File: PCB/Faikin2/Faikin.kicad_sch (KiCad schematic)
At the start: 33 parts, among them J1 1x5, J2 Shelly, Q1 BSS138PS, U2 Barcode, U2 ESP32-S3-MINI-1, U3 MD8942

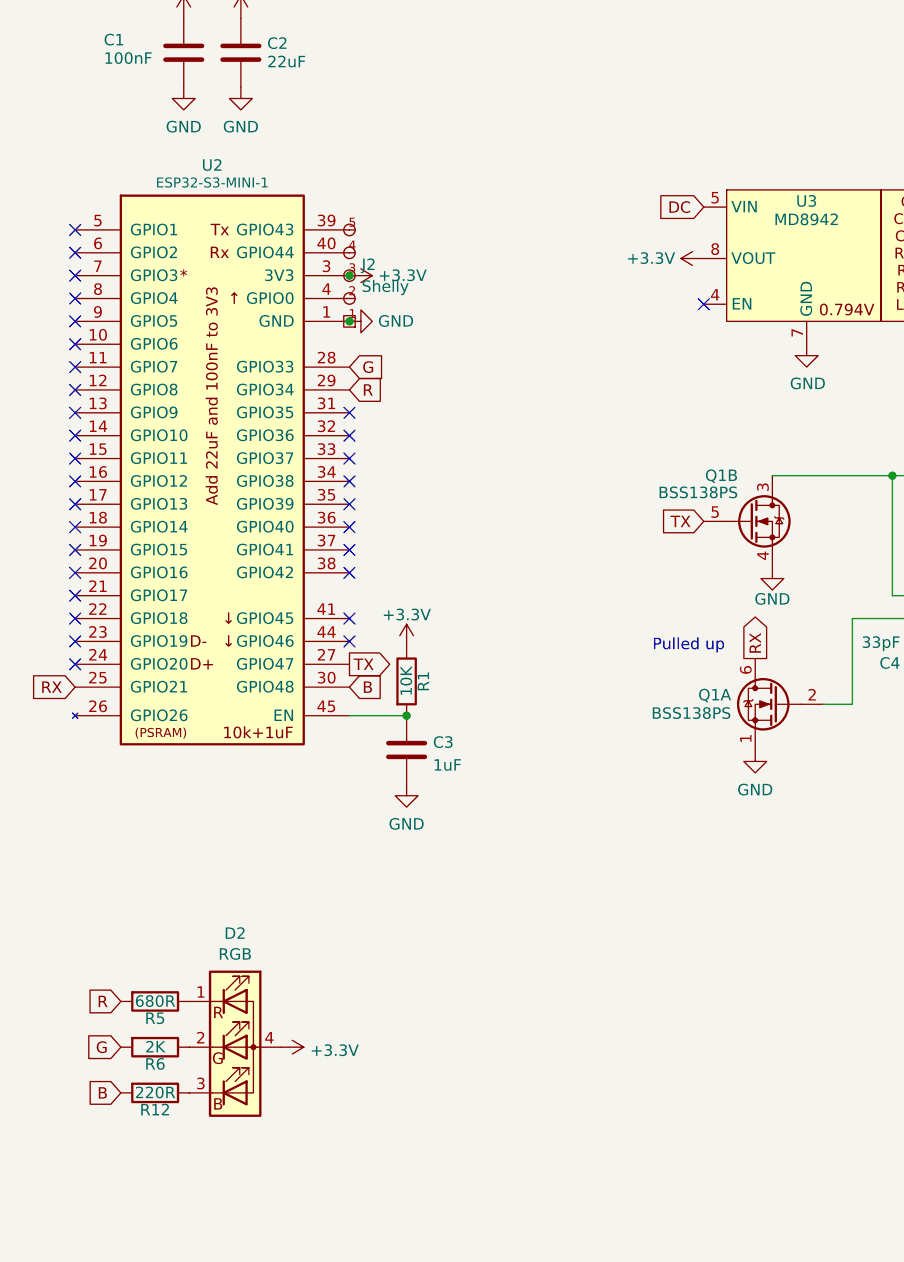
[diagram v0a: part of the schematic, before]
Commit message: Revised for USB connector as well
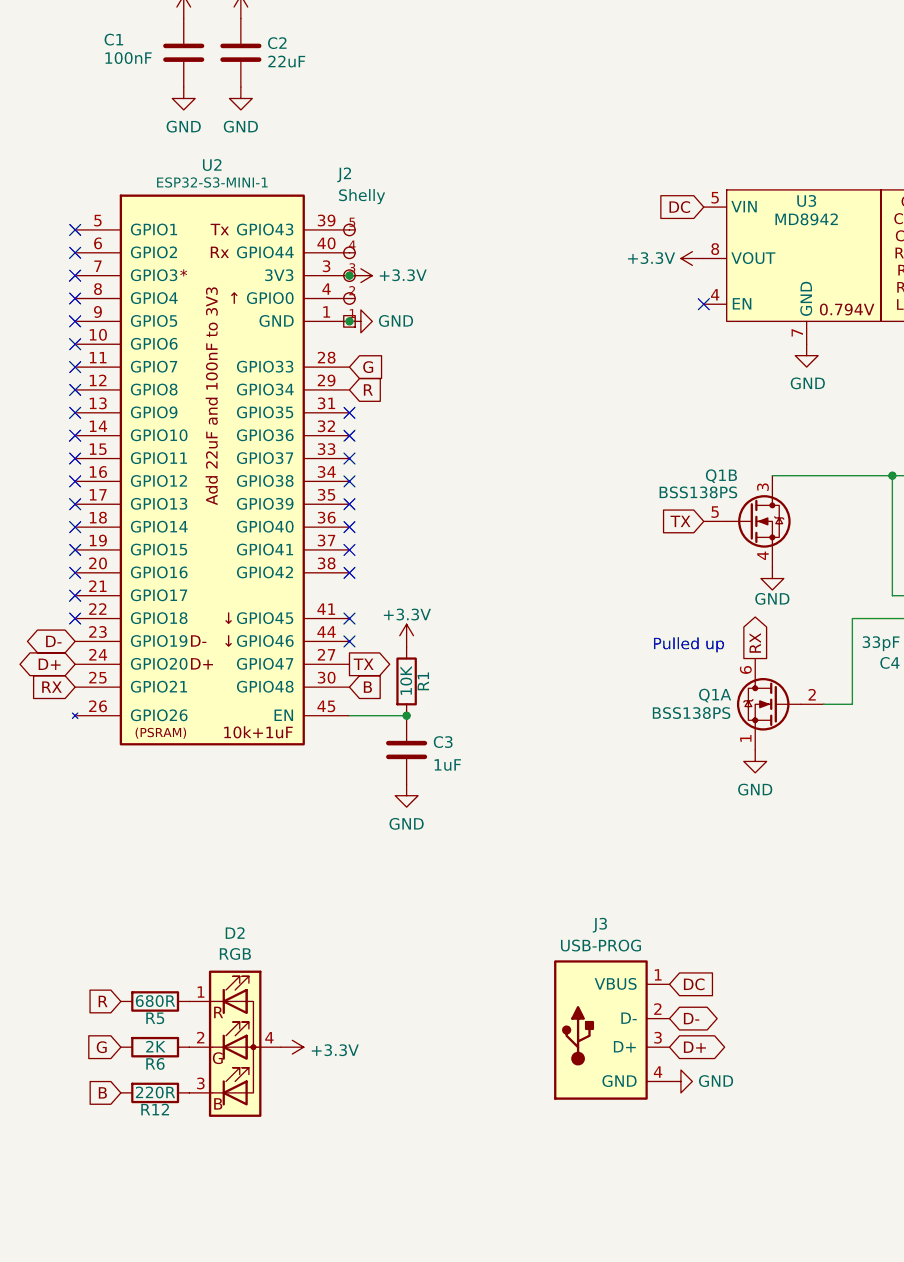
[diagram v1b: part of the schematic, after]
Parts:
- added J3: USB-PROG, RevK:USB-PROG, symbol RevK:USB-PROG
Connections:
- net DC: now also J3.1 (VBUS)
- net GND: now also J3.4 (GND)
- net D-: now reaches U2.23 (GPIO19)
- net D-: now also J3.2 (D-)
- net D+: now reaches U2.24 (GPIO20)
- net D+: now also J3.3 (D+)
- no-connect marks 31 -> 29
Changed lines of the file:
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@@
   (no_connect (at 79.375 71.12))
   (no_connect (at 48.895 60.96))
-  (no_connect (at 48.895 96.52))
   (no_connect (at 79.375 91.44))
   (no_connect (at 48.895 58.42))
@@
   (no_connect (at 48.895 78.74))
   (no_connect (at 48.895 76.2))
-  (no_connect (at 48.895 93.98))
   (no_connect (at 48.895 71.12))
   (no_connect (at 48.895 48.26))
@@
     (effects (font (size 1.27 1.27)) (justify left bottom))
   )
+  (global_label "DC" (shape input) (at 114.935 132.08 0) (fields_autoplaced)
+    (effects (font (size 1.27 1.27)) (justify left))
+    (property "Intersheetrefs" "${INTERSHEET_REFS}" (at 119.806 132.08 0)
+      (effects (font (size 1.27 1.27)) (justify left) hide)
+    )
+  )
+  (global_label "D-" (shape bidirectional) (at 48.895 93.98 180) (fields_autoplaced)
+    (effects (font (size 1.27 1.27)) (justify right))
+    (property "Intersheetrefs" "${INTERSHEET_REFS}" (at 42.7691 93.98 0)
+      (effects (font (size 1.27 1.27)) (justify right) hide)
+    )
+  )
   (global_label "G" (shape input) (at 79.375 63.5 0) (fields_autoplaced)
     (effects (font (size 1.27 1.27)) (justify left))
@@
     )
   )
+  (global_label "D+" (shape bidirectional) (at 48.895 96.52 180) (fields_autoplaced)
+    (effects (font (size 1.27 1.27)) (justify right))
+    (property "Intersheetrefs" "${INTERSHEET_REFS}" (at 42.7691 96.52 0)
+      (effects (font (size 1.27 1.27)) (justify right) hide)
+    )
+  )
   (global_label "TX" (shape input) (at 118.745 80.645 180) (fields_autoplaced)
     (effects (font (size 1.27 1.27)) (justify right))
@@
     )
   )
+  (global_label "D+" (shape bidirectional) (at 114.935 139.065 0) (fields_autoplaced)
+    (effects (font (size 1.27 1.27)) (justify left))
+    (property "Intersheetrefs" "${INTERSHEET_REFS}" (at 121.0609 139.065 0)
+      (effects (font (size 1.27 1.27)) (justify left) hide)
+    )
+  )
   (global_label "DC" (shape output) (at 161.29 86.36 180) (fields_autoplaced)
     (effects (font (size 1.27 1.27)) (justify right))
@@
     )
   )
+  (global_label "D-" (shape bidirectional) (at 114.935 135.89 0) (fields_autoplaced)
+    (effects (font (size 1.27 1.27)) (justify left))
+    (property "Intersheetrefs" "${INTERSHEET_REFS}" (at 121.0609 135.89 0)
+      (effects (font (size 1.27 1.27)) (justify left) hide)
+    )
+  )
   (global_label "RX" (shape input) (at 48.895 99.06 180) (fields_autoplaced)
     (effects (font (size 1.27 1.27)) (justify right))
@@
   )
   (symbol (lib_id "RevK:Shelly") (at 79.375 53.34 0) (unit 1)
-    (in_bom no) (on_board yes) (dnp no) (fields_autoplaced)
-    (property "Reference" "J2" (at 80.7212 52.1279 0)
-      (effects (font (size 1.27 1.27)) (justify left))
-    )
-    (property "Value" "Shelly" (at 80.7212 54.5521 0)
+    (in_bom no) (on_board yes) (dnp no)
+    (property "Reference" "J2" (at 78.105 42.0258 0)
+      (effects (font (size 1.27 1.27)) (justify left))
+    )
+    (property "Value" "Shelly" (at 78.105 44.45 0)
       (effects (font (size 1.27 1.27)) (justify left))
     )
@@
         (path "/46c350bb-7de4-4e81-aafd-4af55e37aab0"
           (reference "V4") (unit 1)
+        )
+      )
+    )
+  )
+  (symbol (lib_id "RevK:USB-PROG") (at 107.315 137.16 0) (unit 1)
+    (in_bom yes) (on_board yes) (dnp no) (fields_autoplaced)
+    (property "Reference" "J3" (at 107.315 125.3957 0)
+      (effects (font (size 1.27 1.27)))
+    )
+    (property "Value" "USB-PROG" (at 107.315 127.8199 0)
+      (effects (font (size 1.27 1.27)))
+    )
+    (property "Footprint" "RevK:USB-PROG" (at 111.125 138.43 0)
+      (effects (font (size 1.27 1.27)) hide)
+    )
+    (property "Datasheet" " ~" (at 111.125 138.43 0)
+      (effects (font (size 1.27 1.27)) hide)
+    )
+    (pin "1")
+    (pin "2")
+    (pin "3")
+    (pin "4")
+    (instances
+      (project "Faikin"
+        (path "/46c350bb-7de4-4e81-aafd-4af55e37aab0"
+          (reference "J3") (unit 1)
         )
       )
@@
         )
       )
+    )
+  )
+  (symbol (lib_id "power:GND") (at 114.935 142.875 90) (unit 1)
+    (in_bom yes) (on_board yes) (dnp no) (fields_autoplaced)
+    (property "Reference" "#PWR0105" (at 121.285 142.875 0)
+      (effects (font (size 1.27 1.27)) hide)
+    )
+    (property "Value" "GND" (at 118.11 142.875 90)
+      (effects (font (size 1.27 1.27)) (justify right))
+    )
+    (property "Footprint" "" (at 114.935 142.875 0)
+      (effects (font (size 1.27 1.27)) hide)
+    )
+    (property "Datasheet" "" (at 114.935 142.875 0)
+      (effects (font (size 1.27 1.27)) hide)
+    )
+    (pin "1")
+    (instances
+      (project "USBA"
+        (path "/2d210a96-f81f-42a9-8bf4-1b43c11086f3"
+          (reference "#PWR0105") (unit 1)
+        )
+      )
+      (project "Faikin"
+        (path "/46c350bb-7de4-4e81-aafd-4af55e37aab0"
+          (reference "#PWR016") (unit 1)
+        )
+      )

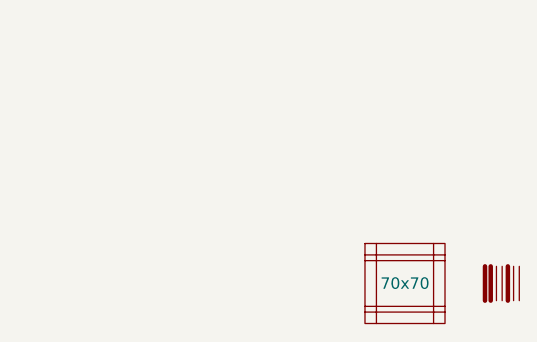
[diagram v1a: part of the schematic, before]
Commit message: Could not do larger board outline
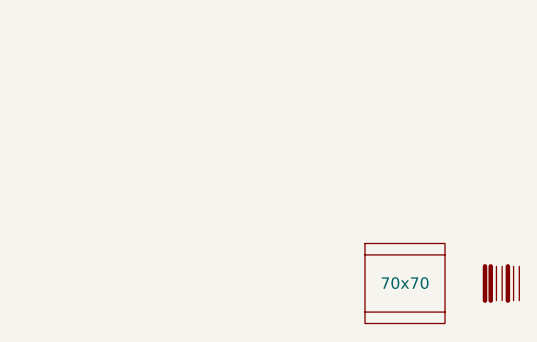
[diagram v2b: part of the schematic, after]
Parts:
- removed V3, V4, V5, V6: ~, RevK:VCUT70, symbol RevK:VCUT
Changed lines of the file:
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@@
-    )
-  )
-  (symbol (lib_id "RevK:VCUT") (at 259.08 174.625 270) (unit 1)
-    (in_bom no) (on_board yes) (dnp no) (fields_autoplaced)
-    (property "Reference" "V4" (at 260.35 174.625 0)
-      (effects (font (size 1.27 1.27)) hide)
-    )
-    (property "Value" "~" (at 259.08 174.625 0)
-      (effects (font (size 1.27 1.27)))
-    )
-    (property "Footprint" "RevK:VCUT70" (at 257.81 174.625 0)
-      (effects (font (size 1.27 1.27)) hide)
-    )
-    (property "Datasheet" "" (at 259.08 174.625 0)
-      (effects (font (size 1.27 1.27)) hide)
-    )
-    (property "Sim.Enable" "0" (at 259.08 174.625 0)
-      (effects (font (size 1.27 1.27)) hide)
-    )
-    (instances
-      (project "Faikin"
-        (path "/46c350bb-7de4-4e81-aafd-4af55e37aab0"
-          (reference "V4") (unit 1)
-        )
-      )
     )
   )
@@
         (path "/46c350bb-7de4-4e81-aafd-4af55e37aab0"
           (reference "J3") (unit 1)
-        )
-      )
-    )
-  )
-  (symbol (lib_id "RevK:VCUT") (at 262.255 177.165 180) (unit 1)
-    (in_bom no) (on_board yes) (dnp no) (fields_autoplaced)
-    (property "Reference" "V6" (at 262.255 178.435 0)
-      (effects (font (size 1.27 1.27)) hide)
-    )
-    (property "Value" "~" (at 262.255 177.165 0)
-      (effects (font (size 1.27 1.27)))
-    )
-    (property "Footprint" "RevK:VCUT70" (at 262.255 175.895 0)
-      (effects (font (size 1.27 1.27)) hide)
-    )
-    (property "Datasheet" "" (at 262.255 177.165 0)
-      (effects (font (size 1.27 1.27)) hide)
-    )
-    (property "Sim.Enable" "0" (at 262.255 177.165 0)
-      (effects (font (size 1.27 1.27)) hide)
-    )
-    (instances
-      (project "Faikin"
-        (path "/46c350bb-7de4-4e81-aafd-4af55e37aab0"
-          (reference "V6") (unit 1)
         )
       )
@@
         (path "/46c350bb-7de4-4e81-aafd-4af55e37aab0"
           (reference "C6") (unit 1)
-        )
-      )
-    )
-  )
-  (symbol (lib_id "RevK:VCUT") (at 262.255 172.085 0) (unit 1)
-    (in_bom no) (on_board yes) (dnp no) (fields_autoplaced)
-    (property "Reference" "V5" (at 262.255 170.815 0)
-      (effects (font (size 1.27 1.27)) hide)
-    )
-    (property "Value" "~" (at 262.255 172.085 0)
-      (effects (font (size 1.27 1.27)))
-    )
-    (property "Footprint" "RevK:VCUT70" (at 262.255 173.355 0)
-      (effects (font (size 1.27 1.27)) hide)
-    )
-    (property "Datasheet" "" (at 262.255 172.085 0)
-      (effects (font (size 1.27 1.27)) hide)
-    )
-    (property "Sim.Enable" "0" (at 262.255 172.085 0)
-      (effects (font (size 1.27 1.27)) hide)
-    )
-    (instances
-      (project "Faikin"
-        (path "/46c350bb-7de4-4e81-aafd-4af55e37aab0"
-          (reference "V5") (unit 1)
         )
       )
@@
         )
       )
-    )
-  )
-  (symbol (lib_id "RevK:VCUT") (at 265.43 174.625 270) (unit 1)
-    (in_bom no) (on_board yes) (dnp no) (fields_autoplaced)
-    (property "Reference" "V3" (at 266.7 174.625 0)
-      (effects (font (size 1.27 1.27)) hide)
-    )
-    (property "Value" "~" (at 265.43 174.625 0)
-      (effects (font (size 1.27 1.27)))
-    )
-    (property "Footprint" "RevK:VCUT70" (at 264.16 174.625 0)
-      (effects (font (size 1.27 1.27)) hide)
-    )
-    (property "Datasheet" "" (at 265.43 174.625 0)
-      (effects (font (size 1.27 1.27)) hide)
-    )
-    (property "Sim.Enable" "0" (at 265.43 174.625 0)
-      (effects (font (size 1.27 1.27)) hide)
-    )
-    (instances
-      (project "Faikin"
-        (path "/46c350bb-7de4-4e81-aafd-4af55e37aab0"
-          (reference "V3") (unit 1)
-        )
-      )

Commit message: Extra cut outs
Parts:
- removed U2: Barcode, RevK:EAN-5060634238151, symbol RevK:Barcode
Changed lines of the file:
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@@
-    )
-  )
-  (symbol (lib_id "RevK:Barcode") (at 273.05 174.625 0) (unit 1)
-    (in_bom no) (on_board yes) (dnp no) (fields_autoplaced)
-    (property "Reference" "U2" (at 273.05 177.8 0)
-      (effects (font (size 1.27 1.27)) hide)
-    )
-    (property "Value" "Barcode" (at 273.05 179.705 0)
-      (effects (font (size 1.27 1.27)) hide)
-    )
-    (property "Footprint" "RevK:EAN-5060634238151" (at 272.415 175.26 0)
-      (effects (font (size 1.27 1.27)) hide)
-    )
-    (property "Datasheet" "" (at 272.415 175.26 0)
-      (effects (font (size 1.27 1.27)) hide)
-    )
-    (property "Note" "Non part, PCB printed" (at 273.05 168.91 0)
-      (effects (font (size 1.27 1.27)) hide)
-    )
-    (instances
-      (project "Faikin"
-        (path "/46c350bb-7de4-4e81-aafd-4af55e37aab0"
-          (reference "U2") (unit 1)
-        )
-      )
     )
   )

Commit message: Pull up
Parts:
- added R1: 10K, RevK:R_0402, symbol Device:R
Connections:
- net +3.3V: now also R1.1
- net RX: now also R1.2
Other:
- note removed: "Pulled up"
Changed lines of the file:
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@@
   (junction (at 79.375 58.42) (diameter 0) (color 0 0 0 0)
+  )
+  (junction (at 117.475 95.885) (diameter 0) (color 0 0 0 0)
   )
   (junction (at 139.7 75.565) (diameter 0) (color 0 0 0 0)
@@
     (stroke (width 0) (type default))
   )
+  (wire (pts (xy 117.475 95.885) (xy 124.46 95.885))
+    (stroke (width 0) (type default))
+  )
+  (wire (pts (xy 113.03 95.885) (xy 117.475 95.885))
+    (stroke (width 0) (type default))
+  )
   (wire (pts (xy 157.48 88.9) (xy 161.29 88.9))
     (stroke (width 0) (type default))
@@
   (wire (pts (xy 143.51 91.44) (xy 149.86 91.44))
     (stroke (width 0) (type default))
-  )
-  (text "Pulled up" (at 113.03 95.25 0)
-    (effects (font (size 1.27 1.27)) (justify left bottom))
   )
   (global_label "DC" (shape input) (at 114.935 132.08 0) (fields_autoplaced)
@@
     )
   )
-  (global_label "RX" (shape output) (at 124.46 95.885 90) (fields_autoplaced)
-    (effects (font (size 1.27 1.27)) (justify left))
-    (property "Intersheetrefs" "${INTERSHEET_REFS}" (at 124.3806 91.0813 90)
-      (effects (font (size 1.27 1.27)) (justify left) hide)
+  (global_label "RX" (shape output) (at 113.03 95.885 180) (fields_autoplaced)
+    (effects (font (size 1.27 1.27)) (justify right))
+    (property "Intersheetrefs" "${INTERSHEET_REFS}" (at 108.2195 95.885 0)
+      (effects (font (size 1.27 1.27)) (justify right) hide)
     )
   )
@@
         (path "/46c350bb-7de4-4e81-aafd-4af55e37aab0"
           (reference "#PWR05") (unit 1)
+        )
+      )
+    )
+  )
+  (symbol (lib_id "Device:R") (at 117.475 92.075 0) (unit 1)
+    (in_bom yes) (on_board yes) (dnp no)
+    (property "Reference" "R1" (at 119.38 92.075 90)
+      (effects (font (size 1.27 1.27)))
+    )
+    (property "Value" "10K" (at 117.475 92.075 90)
+      (effects (font (size 1.27 1.27)))
+    )
+    (property "Footprint" "RevK:R_0402" (at 115.697 92.075 90)
+      (effects (font (size 1.27 1.27)) hide)
+    )
+    (property "Datasheet" "~" (at 117.475 92.075 0)
+      (effects (font (size 1.27 1.27)) hide)
+    )
+    (pin "1")
+    (pin "2")
+    (instances
+      (project "USBA"
+        (path "/2d210a96-f81f-42a9-8bf4-1b43c11086f3"
+          (reference "R1") (unit 1)
+        )
+      )
+      (project "Faikin"
+        (path "/46c350bb-7de4-4e81-aafd-4af55e37aab0"
+          (reference "R4") (unit 1)
+        )
+      )
+      (project "Reference"
+        (path "/825c70b0-4860-42b7-97dc-86bfa46e06fd"
+          (reference "R7") (unit 1)
         )
       )
@@
         )
       )
+    )
+  )
+  (symbol (lib_id "power:+3.3V") (at 117.475 88.265 0) (unit 1)
+    (in_bom yes) (on_board yes) (dnp no) (fields_autoplaced)
+    (property "Reference" "#PWR0106" (at 117.475 92.075 0)
+      (effects (font (size 1.27 1.27)) hide)
+    )
+    (property "Value" "+3.3V" (at 117.475 84.6892 0)
+      (effects (font (size 1.27 1.27)))
+    )
+    (property "Footprint" "" (at 117.475 88.265 0)
+      (effects (font (size 1.27 1.27)) hide)
+    )
+    (property "Datasheet" "" (at 117.475 88.265 0)
+      (effects (font (size 1.27 1.27)) hide)
+    )
+    (pin "1")
+    (instances
+      (project "USBA"
+        (path "/2d210a96-f81f-42a9-8bf4-1b43c11086f3"
+          (reference "#PWR0106") (unit 1)
+        )
+      )
+      (project "Faikin"
+        (path "/46c350bb-7de4-4e81-aafd-4af55e37aab0"
+          (reference "#PWR017") (unit 1)
+        )
+      )

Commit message: Extra supply cap
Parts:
- added C2: 22uF, RevK:C_0402, symbol Device:C
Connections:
- net DC: now also C2.1
- net GND: now also C2.2
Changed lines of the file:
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@@
+    )
+  )
+  (global_label "DC" (shape input) (at 78.74 24.765 90) (fields_autoplaced)
+    (effects (font (size 1.27 1.27)) (justify left))
+    (property "Intersheetrefs" "${INTERSHEET_REFS}" (at 78.74 19.894 90)
+      (effects (font (size 1.27 1.27)) (justify left) hide)
     )
   )
@@
     )
   )
+  (symbol (lib_id "Device:C") (at 78.74 28.575 0) (unit 1)
+    (in_bom yes) (on_board yes) (dnp no) (fields_autoplaced)
+    (property "Reference" "C2" (at 81.661 27.551 0)
+      (effects (font (size 1.27 1.27)) (justify left))
+    )
+    (property "Value" "22uF" (at 81.661 29.599 0)
+      (effects (font (size 1.27 1.27)) (justify left))
+    )
+    (property "Footprint" "RevK:C_0402" (at 79.7052 32.385 0)
+      (effects (font (size 1.27 1.27)) hide)
+    )
+    (property "Datasheet" "~" (at 78.74 28.575 0)
+      (effects (font (size 1.27 1.27)) hide)
+    )
+    (pin "1")
+    (pin "2")
+    (instances
+      (project "USBA"
+        (path "/2d210a96-f81f-42a9-8bf4-1b43c11086f3"
+          (reference "C2") (unit 1)
+        )
+      )
+      (project "Faikin"
+        (path "/46c350bb-7de4-4e81-aafd-4af55e37aab0"
+          (reference "C1") (unit 1)
+        )
+      )
+    )
+  )
   (symbol (lib_id "Device:R") (at 117.475 92.075 0) (unit 1)
     (in_bom yes) (on_board yes) (dnp no)
@@
         )
       )
+    )
+  )
+  (symbol (lib_id "power:GND") (at 78.74 32.385 0) (unit 1)
+    (in_bom yes) (on_board yes) (dnp no) (fields_autoplaced)
+    (property "Reference" "#PWR013" (at 78.74 38.735 0)
+      (effects (font (size 1.27 1.27)) hide)
+    )
+    (property "Value" "GND" (at 78.74 36.8284 0)
+      (effects (font (size 1.27 1.27)))
+    )
+    (property "Footprint" "" (at 78.74 32.385 0)
+      (effects (font (size 1.27 1.27)) hide)
+    )
+    (property "Datasheet" "" (at 78.74 32.385 0)
+      (effects (font (size 1.27 1.27)) hide)
+    )
+    (pin "1")
+    (instances
+      (project "USBA"
+        (path "/2d210a96-f81f-42a9-8bf4-1b43c11086f3"
+          (reference "#PWR013") (unit 1)
+        )
+      )
+      (project "Faikin"
+        (path "/46c350bb-7de4-4e81-aafd-4af55e37aab0"
+          (reference "#PWR018") (unit 1)
+        )
+      )
